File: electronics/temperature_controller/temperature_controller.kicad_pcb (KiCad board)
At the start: 2 copper layers, 139.2 x 91.4 mm, 31 parts, among them J1 Conn_01x03_Male, J2 Conn_01x03_Male, J3 Conn_01x03_Male, J4 Conn_01x03_Male, J5 Conn_01x03_Male, J6 Conn_01x03_Male, K1 RT44xxxx, K2 RT44xxxx, K3 ADW11, K4 ADW11, Q1 2N3904, Q2 2N3904, Q3 2N3904, Q4 2N3904, U1 MC7805CTG, U2 Pico

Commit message: finish board schematics
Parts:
- removed K1, K2: RT44xxxx, Relay_THT:Relay_DPST_Schrack-RT2-FormA_RM5mm
- removed K3, K4: ADW11, Relay_THT:Relay_1P1T_NO_10x24x18.8mm_Panasonic_ADW11xxxxW_THT
- removed RV1, RV2: Varistor, Varistor:RV_Disc_D15.5mm_W4.2mm_P7.5mm
- added D9: 1N5817, Diode_THT:D_DO-41_SOD81_P10.16mm_Horizontal, F.Cu at (160.4, 76.2)
- added H1: MountingHole, MountingHole:MountingHole_3.2mm_M3_Pad_TopBottom, F.Cu at (159.4, 103.3)
- added H2: MountingHole, MountingHole:MountingHole_3.2mm_M3_Pad_TopBottom, F.Cu at (149.9, 111.8)
- added H3: MountingHole, MountingHole:MountingHole_3.2mm_M3_Pad_TopBottom, F.Cu at (172.4, 93.0)
- added H4: MountingHole, MountingHole:MountingHole_3.2mm_M3_Pad_TopBottom, F.Cu at (183.5, 78.1)
- added J10: 1217861-1, ProjectComponents:TE_1217861-1, F.Cu at (77.5, 16.8)
- added J11: 1217861-1, ProjectComponents:TE_1217861-1, F.Cu at (91.9, 16.8)
- added J12: 1217861-1, ProjectComponents:TE_1217861-1, F.Cu at (82.5, 16.8)
- added J13: 1217861-1, ProjectComponents:TE_1217861-1, F.Cu at (86.9, 29.0)
- added J14: 1217861-1, ProjectComponents:TE_1217861-1, F.Cu at (77.2, 29.0)
- added J15: 1217861-1, ProjectComponents:TE_1217861-1, F.Cu at (91.9, 28.7)
- added J16: 1217861-1, ProjectComponents:TE_1217861-1, F.Cu at (81.9, 29.0)
- added J17: Conn_01x03_Male, Connector_PinHeader_2.54mm:PinHeader_1x03_P2.54mm_Vertical, F.Cu at (143.6, 105.7)
- added J18: 1217861-1, ProjectComponents:TE_1217861-1, F.Cu at (134.6, 88.4)
- added J19: 1217861-1, ProjectComponents:TE_1217861-1, F.Cu at (161.6, 97.0)
- added J20: 1217861-1, ProjectComponents:TE_1217861-1, F.Cu at (173.2, 86.7)
- added J21: 1217861-1, ProjectComponents:TE_1217861-1, F.Cu at (174.8, 80.7)
- added J22: Conn_01x15_Male, Connector_PinHeader_2.54mm:PinHeader_1x15_P2.54mm_Vertical, F.Cu at (156.7, 4.32)
- added J23: Conn_01x15_Male, Connector_PinHeader_2.54mm:PinHeader_1x15_P2.54mm_Vertical, F.Cu at (202.2, 4.32)
- added J24: TB006-508-02BE, ProjectComponents:CUI_TB006-508-02BE, F.Cu at (217.7, 33.5)
- added J25: TB006-508-02BE, ProjectComponents:CUI_TB006-508-02BE, F.Cu at (232.6, 15.9)
- added J26: TB006-508-02BE, ProjectComponents:CUI_TB006-508-02BE, F.Cu at (244.3, 15.9)
- added J27: TB006-508-02BE, ProjectComponents:CUI_TB006-508-02BE, F.Cu at (232.6, 26.6)
- added J28: TB006-508-02BE, ProjectComponents:CUI_TB006-508-02BE, F.Cu at (244.3, 26.6)
- added J29: TB006-508-02BE, ProjectComponents:CUI_TB006-508-02BE, F.Cu at (256.0, 15.9)
- added J30: Conn_01x03_Male, Connector_PinHeader_2.54mm:PinHeader_1x03_P2.54mm_Vertical, F.Cu at (230.4, -4.83)
- added J7: 1217861-1, ProjectComponents:TE_1217861-1, F.Cu at (91.7, 40.6)
- added J8: 1217861-1, ProjectComponents:TE_1217861-1, F.Cu at (87.1, 40.6)
- added J9: 1217861-1, ProjectComponents:TE_1217861-1, F.Cu at (87.1, 16.8)
- added Q5: 2N3904, Package_TO_SOT_THT:TO-92_Inline, F.Cu at (155.9, 111.1)
- added Q6: 2N3904, Package_TO_SOT_THT:TO-92_Inline, F.Cu at (165.4, 102.6)
- added R12: 150, Resistor_SMD:R_0805_2012Metric_Pad1.20x1.40mm_HandSolder, F.Cu at (185.3, 93.3)
- added R13: 150, Resistor_SMD:R_0805_2012Metric_Pad1.20x1.40mm_HandSolder, F.Cu at (190.0, 89.1)
- added R14: 10k, Resistor_SMD:R_0805_2012Metric_Pad1.20x1.40mm_HandSolder, F.Cu at (167.6, 114.3)
- added R15: 10k, Resistor_SMD:R_0805_2012Metric_Pad1.20x1.40mm_HandSolder, F.Cu at (178.2, 102.2)
- added R16: 1k, Resistor_SMD:R_0805_2012Metric_Pad1.20x1.40mm_HandSolder, F.Cu at (173.5, 106.9)
- added R17: 1k, Resistor_SMD:R_0805_2012Metric_Pad1.20x1.40mm_HandSolder, F.Cu at (182.9, 99.2)
- added R3: 10k, Resistor_SMD:R_0805_2012Metric_Pad1.20x1.40mm_HandSolder, F.Cu at (178.7, 96.3)
- added R4: 10k, Resistor_SMD:R_0805_2012Metric_Pad1.20x1.40mm_HandSolder, F.Cu at (185.3, 90.3)
- added R5: 1k, Resistor_SMD:R_0805_2012Metric_Pad1.20x1.40mm_HandSolder, F.Cu at (162.8, 114.3)
- added R6: 1k, Resistor_SMD:R_0805_2012Metric_Pad1.20x1.40mm_HandSolder, F.Cu at (172.3, 104.0)
- added R7: 1k, Resistor_SMD:R_0805_2012Metric_Pad1.20x1.40mm_HandSolder, F.Cu at (178.2, 99.2)
- added R8: 1k, Resistor_SMD:R_0805_2012Metric_Pad1.20x1.40mm_HandSolder, F.Cu at (168.7, 106.9)
- added R9: 4k7, Resistor_SMD:R_0805_2012Metric_Pad1.20x1.40mm_HandSolder, F.Cu at (174.8, 75.6)
- added U3: BOB-12009, ProjectComponents:CONV_BOB-12009, F.Cu at (221.8, 18.9)
- C1, C2: footprint Capacitor_THT:C_Rect_L18.0mm_W9.0mm_P15.00mm_FKS3_FKP3 -> Capacitor_THT:C_Disc_D8.0mm_W2.5mm_P5.00mm
- D1, D4: value 1N4148TA -> LED; footprint digikey-footprints:DO-35 -> LED_THT:LED_D3.0mm
- D2, D3: value 1N4148TA -> 1N5817; footprint digikey-footprints:DO-35 -> Diode_THT:D_DO-41_SOD81_P10.16mm_Horizontal
- D7, D8: value LED -> 1N5817; footprint LED_THT:LED_D3.0mm -> Diode_THT:D_DO-41_SOD81_P10.16mm_Horizontal
- J1, J2: value Conn_01x03_Male -> SJ1-3523N; footprint TerminalBlock_Phoenix:TerminalBlock_Phoenix_MKDS-3-3-5.08_1x03_P5.08mm_Horizontal -> ProjectComponents:CUI_SJ1-3523N
- J3: footprint TerminalBlock_Phoenix:TerminalBlock_Phoenix_MKDS-3-3-5.08_1x03_P5.08mm_Horizontal -> Connector_PinHeader_2.54mm:PinHeader_1x03_P2.54mm_Vertical
- J4: value Conn_01x03_Male -> SJ1-3523N; footprint Connector_PinHeader_2.54mm:PinHeader_1x03_P2.54mm_Vertical -> ProjectComponents:CUI_SJ1-3523N
- J5, J6: value Conn_01x03_Male -> 1217861-1; footprint Connector_PinHeader_2.54mm:PinHeader_1x03_P2.54mm_Vertical -> ProjectComponents:TE_1217861-1
- PS1: value IRM-10-12 -> IRM-02-12; footprint Converter_ACDC:Converter_ACDC_MeanWell_IRM-10-xx_THT -> Converter_ACDC:Converter_ACDC_MeanWell_IRM-02-xx_THT
- Q1, Q2: footprint digikey-footprints:TO-92-3 -> Package_TO_SOT_THT:TO-92_Inline
- Q3, Q4: value 2N3904 -> IRF9Z34NPBF; footprint digikey-footprints:TO-92-3 -> Package_TO_SOT_THT:TO-220-3_Vertical
- R1, R2: value R -> 150; footprint Resistor_THT:R_Axial_DIN0516_L15.5mm_D5.0mm_P25.40mm_Horizontal -> Resistor_SMD:R_0805_2012Metric_Pad1.20x1.40mm_HandSolder
- U1: value MC7805CTG -> MC7805CT-BPMS-ND; footprint digikey-footprints:TO-220-3 -> Package_TO_SOT_THT:TO-220-3_Vertical
- U2: value Pico -> NodeMCU1.0(ESP-12E); footprint MCU_RaspberryPi_and_Boards:RPi_Pico_SMD_TH -> ESP8266:NodeMCU1.0(12-E)
- moved J5 173.5 mm to (77.7, 40.7), turned to 90 degrees
- moved R1 170.3 mm to (189.9, 75.6)
- moved R2 151.4 mm to (189.9, 78.5)
- moved J4 147.1 mm to (79.5, 84.3), turned to 0 degrees
- moved C1 123.8 mm to (160.8, 86.4), turned to 0 degrees
- moved PS1 109.6 mm to (106.4, 16.5)
- moved Q2 106.6 mm to (179.9, 86.3), turned to 0 degrees
- moved U2 106.6 mm to (178.8, 22.1), turned to 0 degrees
- moved D5 98.1 mm to (170.7, 85.7), turned to 0 degrees
- moved D1 90.3 mm to (186.1, 84.8), turned to 0 degrees
- moved J2 87.0 mm to (79.5, 99.6), turned to 0 degrees
- moved J6 85.0 mm to (82.4, 40.6), turned to 90 degrees
- moved D2 83.9 mm to (144.8, 90.9), turned to 0 degrees
- moved Q1 82.4 mm to (178.4, 92.3), turned to 0 degrees
- moved J3 82.4 mm to (114.4, 97.6), turned to 0 degrees
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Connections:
- C1 pad 2: Net-(C1-Pad2) -> GND
- C2 pad 1: Net-(C2-Pad1) -> +12V
- C2 pad 2: Net-(C2-Pad2) -> GND
- D5 pad 1: Net-(D2-PadA) -> Net-(D5-Pad1)
- D6 pad 1: Net-(D1-PadA) -> Net-(D6-Pad1)
- D7 pad 1: Net-(D3-PadA) -> +12V
- D7 pad 2: +12V -> Net-(D7-Pad2)
- D8 pad 1: Net-(D8-Pad1) -> +12V
- D8 pad 2: +12V -> Net-(D8-Pad2)
- J1 pad 1: LIVE -> GND
- J1 pad 2: NEUTRAL -> +5V
- J1 pad 3: Earth -> ONEWIRE
- J2 pad 1: Net-(C1-Pad1) -> GND
- J2 pad 2: Net-(J2-Pad2) -> +5V
- J2 pad 3: Earth -> ONEWIRE
- J3 pad 1: Net-(C2-Pad1) -> GND
- J3 pad 2: Net-(J3-Pad2) -> Net-(D2-Pad1)
- J3 pad 3: Earth -> Net-(J3-Pad3)
- J4 pad 2: Net-(J4-Pad2) -> +5V
- J4 pad 3: Net-(J4-Pad3) -> ONEWIRE
- J5 pad 1: GND -> EARTH
- J5 pad 2: Net-(J5-Pad2) -> EARTH
- J6 pad 1: Net-(J6-Pad1) -> EARTH
- J6 pad 2: GND -> EARTH
- Q1 pad 2: Net-(D1-PadA) -> Net-(Q1-Pad2)
- Q1 pad 3: HEAT -> Net-(Q1-Pad3)
- Q2 pad 2: Net-(D2-PadA) -> Net-(Q2-Pad2)
- Q2 pad 3: COOL -> Net-(Q2-Pad3)
- Q3 pad 1: GND -> Net-(Q1-Pad3)
- Q3 pad 2: Net-(D3-PadA) -> Net-(D2-Pad1)
- Q3 pad 3: FAN1 -> +12V
- Q4 pad 1: GND -> Net-(Q2-Pad3)
- Q4 pad 2: Net-(D4-PadA) -> Net-(D3-Pad1)
- Q4 pad 3: FAN2 -> +12V
- R1 pad 1: Net-(C1-Pad2) -> Net-(Q1-Pad2)
- R1 pad 2: Net-(J2-Pad2) -> FAN1
- R2 pad 1: Net-(C2-Pad2) -> Net-(Q2-Pad2)
- R2 pad 2: Net-(J3-Pad2) -> FAN2
- U1 pad 3: +5V -> Net-(C1-Pad1)
- U2 pad 10: Net-(U2-Pad10) -> GND
- U2 pad 12: FAN2 -> Net-(J22-Pad12)
- U2 pad 13: GND -> Net-(J22-Pad13)
- U2 pad 14: Net-(U2-Pad14) -> GND
- U2 pad 15: Net-(U2-Pad15) -> +5V
- U2 pad 17: FAN1 -> GND
- U2 pad 18: GND -> Net-(J23-Pad13)
- U2 pad 20: Net-(U2-Pad20) -> FAN2
- U2 pad 22: Net-(U2-Pad22) -> ONEWIRE
- U2 pad 23: GND -> COOL
- U2 pad 24: COOL -> GND
- U2 pad 26: Net-(U2-Pad26) -> FAN1
- U2 pad 28: GND -> Net-(J23-Pad3)
- U2 pad 29: HEAT -> Net-(J23-Pad2)
- U2 pad 3: GND -> Net-(J22-Pad3)
- U2 pad 30: Net-(U2-Pad30) -> HEAT
- U2 pad 8: GND -> Net-(J22-Pad8)
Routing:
- net LIVE: track 85.6 -> 0.00 mm
- net Net-(J2-Pad2): track 47.3 -> 0.00 mm
- net Net-(C1-Pad1): track 40.5 -> 0.00 mm
- net Net-(J3-Pad2): track 40.3 -> 0.00 mm
- net Net-(C2-Pad1): track 34.9 -> 0.00 mm
- net Net-(C2-Pad2): track 8.23 -> 0.00 mm
- net Net-(C1-Pad2): track 8.23 -> 0.00 mm
- removed copper zone on B.Cu, net Earth
- removed copper zone on B.Cu, net GND
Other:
- board size 139.2 x 91.4 mm -> 1.2 x 12 mm

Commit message: update footprints, schematic and start board layout
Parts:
- removed the J10 at (77.5, 16.8)
- removed the J11 at (91.9, 16.8)
- removed the J12 at (82.5, 16.8)
- removed the J26 at (244.3, 15.9)
- removed J27: TB006-508-02BE, ProjectComponents:CUI_TB006-508-02BE
- removed the J7 at (91.7, 40.6)
- removed the J8 at (87.1, 40.6)
- removed the J9 at (87.1, 16.8)
- added C3: C, Capacitor_THT:C_Disc_D8.0mm_W2.5mm_P5.00mm, F.Cu at (179.8, -11.2)
- added C4: C, Capacitor_THT:C_Disc_D8.0mm_W2.5mm_P5.00mm, F.Cu at (165.9, -0.97)
- added D10: 1N5817, Diode_THT:D_DO-41_SOD81_P10.16mm_Horizontal, F.Cu at (243.1, 84.6)
- added D11: 1N5817, Diode_THT:D_DO-41_SOD81_P10.16mm_Horizontal, F.Cu at (14.0, -15.2)
- added J13: Conn_01x15_Male, Connector_PinHeader_2.54mm:PinHeader_1x15_P2.54mm_Vertical, F.Cu at (57.9, -92.7)
- added J14: SJ1-3523N, ProjectComponents:CUI_SJ1-3523N, F.Cu at (80.3, -4.83)
- added J16: SJ1-3523N, ProjectComponents:CUI_SJ1-3523N, F.Cu at (67.1, -4.83)
- added J17: Conn_01x03_Male, Connector_PinHeader_2.54mm:PinHeader_1x03_P2.54mm_Vertical, F.Cu at (283.8, 89.5)
- added J18: 1217861-1, ProjectComponents:TE_1217861-1, F.Cu at (22.4, -9.40)
- added J21: 1217861-1, ProjectComponents:TE_1217861-1, F.Cu at (30.5, -85.1)
- added J22: 1217861-1, ProjectComponents:TE_1217861-1, F.Cu at (30.7, -90.4)
- added J23: 1217861-1, ProjectComponents:TE_1217861-1, F.Cu at (30.5, -79.0)
- added J30: 1217861-1, ProjectComponents:TE_1217861-1, F.Cu at (19.8, -84.5)
- added J31: 1217861-1, ProjectComponents:TE_1217861-1, F.Cu at (19.8, -96.5)
- added J32: 1217861-1, ProjectComponents:TE_1217861-1, F.Cu at (22.6, -4.06)
- added J33: 1217861-1, ProjectComponents:TE_1217861-1, F.Cu at (4.57, -19.8)
- added J4: 1217861-1, ProjectComponents:TE_1217861-1, F.Cu at (-10.9, 25.7)
- added J40: 1217861-1, ProjectComponents:TE_1217861-1, F.Cu at (6.35, -84.5)
- added J41: 1217861-1, ProjectComponents:TE_1217861-1, F.Cu at (6.35, -78.5)
- added PS1: IRM-10-12, Converter_ACDC:Converter_ACDC_MeanWell_IRM-10-xx_THT, F.Cu at (15.0, -70.0)
- added U4: MC7805CT-BPMS-ND, Package_TO_SOT_THT:TO-220-3_Vertical, F.Cu at (193.8, -19.8)
- D5: renamed from D4; value LED -> 1N5817; footprint LED_THT:LED_D3.0mm -> Diode_THT:D_DO-41_SOD81_P10.16mm_Horizontal
- D7: value 1N5817 -> LED; footprint Diode_THT:D_DO-41_SOD81_P10.16mm_Horizontal -> LED_THT:LED_D3.0mm
- J1: value SJ1-3523N -> Conn_02x03_Odd_Even; footprint ProjectComponents:CUI_SJ1-3523N -> Connector_PinHeader_2.54mm:PinHeader_2x03_P2.54mm_Vertical
- J15: value 1217861-1 -> SJ1-3523N; footprint ProjectComponents:TE_1217861-1 -> ProjectComponents:CUI_SJ1-3523N
- J19: renamed from J22; value Conn_01x15_Male -> 1217861-1; footprint Connector_PinHeader_2.54mm:PinHeader_1x15_P2.54mm_Vertical -> ProjectComponents:TE_1217861-1
- J2: value SJ1-3523N -> Conn_01x03_Male; footprint ProjectComponents:CUI_SJ1-3523N -> Connector_PinHeader_2.54mm:PinHeader_1x03_P2.54mm_Vertical
- J24, J25, J28, J29: value TB006-508-02BE -> 1217861-1; footprint ProjectComponents:CUI_TB006-508-02BE -> ProjectComponents:TE_1217861-1
- J26: renamed from J23; value Conn_01x15_Male -> 1217861-1; footprint Connector_PinHeader_2.54mm:PinHeader_1x15_P2.54mm_Vertical -> ProjectComponents:TE_1217861-1
- J3: renamed from J4; value SJ1-3523N -> Conn_02x08_Odd_Even; footprint ProjectComponents:CUI_SJ1-3523N -> Connector_PinHeader_2.54mm:PinHeader_2x08_P2.54mm_Vertical
- J39: renamed from J30; value Conn_01x03_Male -> 1217861-1; footprint Connector_PinHeader_2.54mm:PinHeader_1x03_P2.54mm_Vertical -> ProjectComponents:TE_1217861-1
- J6: value 1217861-1 -> Conn_01x03_Male; footprint ProjectComponents:TE_1217861-1 -> Connector_PinHeader_2.54mm:PinHeader_1x03_P2.54mm_Vertical
- J8: renamed from J17; value Conn_01x03_Male -> Conn_01x15_Male; footprint Connector_PinHeader_2.54mm:PinHeader_1x03_P2.54mm_Vertical -> Connector_PinHeader_2.54mm:PinHeader_1x15_P2.54mm_Vertical
- R11: renamed from R13; value 150 -> 10k
- R13: renamed from R15; value 10k -> 1k
- R15: renamed from R17; value 1k -> 4k7
- R7: value 1k -> 1k (DNP)
- R9: value 4k7 -> 150
- U1: renamed from U2; value NodeMCU1.0(ESP-12E) -> LD1117S33TR_SOT223; footprint ESP8266:NodeMCU1.0(12-E) -> Package_TO_SOT_SMD:SOT-223-3_TabPin2
- U2: renamed from U1; value MC7805CT-BPMS-ND -> NodeMCU1.0(ESP-12E); footprint Package_TO_SOT_THT:TO-220-3_Vertical -> ESP8266:NodeMCU1.0(12-E)
- moved J29 259.0 mm to (19.8, -90.5), turned to 180 degrees
- moved J28 247.8 mm to (19.8, -78.5), turned to 180 degrees
- moved J39 243.1 mm to (5.33, -96.8), turned to 180 degrees
- moved J24 227.7 mm to (30.7, -96.5), turned to 180 degrees
- moved J25 226.3 mm to (7.11, -3.81)
- moved J5 219.5 mm to (293.4, 81.6), turned to 0 degrees
- moved J6 214.0 mm to (293.4, 76.9), turned to 0 degrees
- moved U3 207.8 mm to (46.2, -92.2), turned to 90 degrees
- moved J11 199.3 mm to (-11.2, 10.9), turned to 180 degrees
- moved J10 198.1 mm to (-10.9, -0.25)
- moved J26 195.3 mm to (7.37, -9.40), turned to 180 degrees
- moved J8 174.6 mm to (57.9, -46.5), turned to 90 degrees
- moved U2 173.5 mm to (75.7, -68.3), turned to 90 degrees
- moved J9 167.9 mm to (-11.2, 5.08), turned to 180 degrees
- moved D3 155.9 mm to (54.4, -36.1), turned to 180 degrees
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- renumbered D5 to D1, D1 to D2, D2 to D3, D3 to D4, J19 to J10, J20 to J11, J21 to J12, J13 to J35, J14 to J36, J16 to J38, J3 to J7, J18 to J9, PS1 to PS2, R12 to R10, R14 to R12, R16 to R14
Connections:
- C1 pad 1: Net-(C1-Pad1) -> +12V
- C2 pad 1: +12V -> Net-(C2-Pad1)
- D1 pad 2: +12V -> Net-(D1-Pad2)
- D3 pad 1: Net-(D2-Pad1) (its old number) -> +3V3
- D3 pad 2: GND -> Net-(C2-Pad1)
- D4 pad 1: Net-(D3-Pad1) -> Net-(D4-Pad1)
- D5 pad 1: Net-(D4-Pad1) -> Net-(D5-Pad1)
- D5 pad 2: +12V -> GND
- D7 pad 1: +12V -> Net-(D7-Pad1)
- D7 pad 2: Net-(D7-Pad2) -> +12V
- D9 pad 1: +5V -> +12V
- D9 pad 2: Net-(C1-Pad1) -> Net-(D9-Pad2)
- J1 pad 1: GND -> AUXO
- J1 pad 2: +5V -> AUXO
- J1 pad 3: ONEWIRE -> Net-(J1-Pad3)
- J10 pad 1: Net-(D7-Pad2) -> Net-(D8-Pad2)
- J10 pad 2: Net-(D7-Pad2) -> Net-(D8-Pad2)
- J12 pad 1: Net-(D8-Pad2) -> Net-(D9-Pad2)
- J12 pad 2: Net-(D8-Pad2) -> Net-(D9-Pad2)
- J15 pad 1: LIVE -> GND
- J15 pad 2: LIVE -> +5V
- J19 pad 1: Net-(J22-Pad1) -> GND
- J19 pad 2: Net-(J22-Pad2) -> GND
- J2 pad 1: GND -> +5V
- J2 pad 2: +5V -> Net-(D1-Pad2)
- J2 pad 3: ONEWIRE -> +12V
- J24 pad 1: +5V -> EARTH
- J24 pad 2: GND -> EARTH
- J25 pad 2: GND -> +5V
- J26 pad 1: HEAT -> +5V
- J26 pad 2: Net-(J23-Pad2) -> +5V
- J28 pad 1: +12V -> NEUTRAL
- J28 pad 2: GND -> NEUTRAL
- J29 pad 1: +12V -> NEUTRAL
- J29 pad 2: GND -> NEUTRAL
- J3 pad 2: +5V -> +3V3
- J3 pad 3: ONEWIRE -> Net-(J1-Pad3)
- J35 pad 1: LIVE -> +12V
- J35 pad 2: LIVE -> +12V
- J36 pad 1: LIVE -> +12V
- J36 pad 2: LIVE -> +12V
- J39 pad 1: +5V -> LIVE
- J39 pad 2: Net-(J30-Pad2) -> LIVE
- J5 pad 1: EARTH -> GND
- J5 pad 2: EARTH -> GND
- J6 pad 1: EARTH -> GND
- J6 pad 2: EARTH -> Net-(D4-Pad1)
- J7 pad 2: Net-(D2-Pad1) (its old number) -> Net-(D5-Pad1)
- J8 pad 1: GND -> Net-(J8-Pad1)
- J8 pad 2: Net-(D3-Pad1) -> Net-(J8-Pad2)
- J8 pad 3: Net-(J17-Pad3) -> Net-(J8-Pad3)
- PS2 pad 4: +12V -> Net-(D11-Pad2)
- Q3 pad 2: Net-(D2-Pad1) (its old number) -> Net-(D4-Pad1)
- Q3 pad 3: +12V -> Net-(D1-Pad2)
- Q4 pad 2: Net-(D3-Pad1) -> Net-(D5-Pad1)
- Q5 pad 3: Net-(D7-Pad2) -> Net-(D8-Pad2)
- Q6 pad 3: Net-(D8-Pad2) -> Net-(D9-Pad2)
- R1 pad 2: FAN1 -> AUX0
- R10 pad 1: Net-(Q5-Pad2) -> Net-(Q6-Pad2)
- R10 pad 2: HEAT -> COOL
- R11 pad 1: Net-(Q6-Pad2) -> GND
- R11 pad 2: COOL -> Net-(Q5-Pad2)
- R12 pad 2: Net-(Q5-Pad2) -> Net-(Q6-Pad2)
- R13 pad 1: GND -> Net-(D6-Pad1)
- R13 pad 2: Net-(Q6-Pad2) -> Net-(D8-Pad2)
- R14 pad 1: Net-(D4-Pad1) -> Net-(D7-Pad1)
- R14 pad 2: Net-(D7-Pad2) -> Net-(D9-Pad2)
- R15 pad 1: Net-(D6-Pad1) -> +5V
- R15 pad 2: Net-(D8-Pad2) -> ONEWIRE
- R2 pad 2: FAN2 -> FAN
- R7 pad 2: +12V -> Net-(D1-Pad2)
- R9 pad 1: +5V -> Net-(Q5-Pad2)
- R9 pad 2: ONEWIRE -> HEAT
- U1 pad 1: Net-(J22-Pad1) -> GND
- U1 pad 2: Net-(J22-Pad2) -> Net-(C2-Pad1)
- U1 pad 3: Net-(J22-Pad3) -> +12V
- U2 pad 1: +12V -> Net-(J8-Pad1)
- U2 pad 2: GND -> Net-(J8-Pad2)
- U2 pad 3: Net-(C1-Pad1) -> Net-(J8-Pad3)
- U3 pad HV: Net-(J30-Pad2) -> Net-(J17-Pad2)
- U3 pad LV: Net-(J23-Pad6) -> Net-(J13-Pad6)
- U3 pad LV1: Net-(J23-Pad2) -> SCL
- U3 pad LV2: Net-(J23-Pad3) -> SDA
- U3 pad LV3: Net-(J23-Pad4) -> Net-(J13-Pad4)
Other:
- board size 1.2 x 12 mm -> 100 x 100 mm

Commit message: finished layout move to bluetooth shield
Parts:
- removed C1, C2: C, Capacitor_THT:C_Disc_D8.0mm_W2.5mm_P5.00mm
- removed D11: 1N5817, Diode_THT:D_DO-41_SOD81_P10.16mm_Horizontal
- removed J13, J8: Conn_01x15_Male, Connector_PinHeader_2.54mm:PinHeader_1x15_P2.54mm_Vertical
- removed J18, J19: 1217861-1, ProjectComponents:TE_1217861-1
- removed U1: LD1117S33TR_SOT223, Package_TO_SOT_SMD:SOT-223-3_TabPin2
- D10, D3, D4, D5, D8, D9: value 1N5817 -> ‎DSS13UTR‎; footprint Diode_THT:D_DO-41_SOD81_P10.16mm_Horizontal -> ProjectComponents:D_SOD-123F
- moved J6 271.3 mm to (85.0, -96.9), turned to 270 degrees
- moved J17 257.5 mm to (81.3, -69.6), turned to 270 degrees
- moved J5 257.5 mm to (97.0, -85.0), turned to 90 degrees
- moved D5 253.6 mm to (44.9, -95.0), turned to 270 degrees
- moved H2 252.6 mm to (5.00, -95.0)
- moved R14 241.6 mm to (51.6, -81.0)
- moved R12 241.2 mm to (51.6, -77.0)
- moved Q5 240.1 mm to (43.9, -85.0), turned to 90 degrees
- moved Q3 238.4 mm to (85.0, -92.1), turned to 180 degrees
- moved D10 237.1 mm to (28.8, -17.0), turned to 90 degrees
- moved R8 233.4 mm to (69.5, -85.2), turned to 180 degrees
- moved R13 230.7 mm to (37.9, -81.0)
- moved R5 229.5 mm to (88.0, -85.3)
- moved D6 229.1 mm to (38.9, -87.0), turned to 180 degrees
- moved R11 225.2 mm to (37.9, -77.0)
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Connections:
- net Net-(J3-Pad10) renamed MISO
- net Net-(J3-Pad12) renamed SCLK
- net Net-(J3-Pad6) renamed MOSI
- net Net-(J3-Pad8) renamed CS
- D10 pad 1: +5V -> +12V
- D10 pad 2: Net-(C3-Pad1) -> Net-(D10-Pad2)
- D3 pad 1: +3V3 -> Net-(D3-Pad1)
- D3 pad 2: Net-(C2-Pad1) -> GND
- D5 pad 1: Net-(D5-Pad1) -> +12V
- D5 pad 2: GND -> Net-(D5-Pad2)
- D9 pad 1: +12V -> +5V
- D9 pad 2: Net-(D9-Pad2) -> Net-(C3-Pad1)
- J10 pad 1: Net-(D8-Pad2) -> Net-(D5-Pad2)
- J10 pad 2: Net-(D8-Pad2) -> Net-(D5-Pad2)
- J12 pad 1: Net-(D9-Pad2) -> Net-(D8-Pad2)
- J12 pad 2: Net-(D9-Pad2) -> Net-(D8-Pad2)
- J3 pad 14: GND -> +12V
- J3 pad 15: +3V3 -> +5V
- J3 pad 2: +3V3 -> +12V
- J3 pad 9: +3V3 -> +5V
- J4 pad 1: Net-(D4-Pad1) -> Net-(D3-Pad1)
- J4 pad 2: Net-(D4-Pad1) -> Net-(D3-Pad1)
- J6 pad 2: Net-(D4-Pad1) -> Net-(D3-Pad1)
- J7 pad 2: Net-(D5-Pad1) -> Net-(D4-Pad1)
- PS1 pad 4: Net-(D11-Pad2) -> Net-(D10-Pad2)
- PS2 pad 4: Net-(D11-Pad2) -> Net-(D10-Pad2)
- Q3 pad 2: Net-(D4-Pad1) -> Net-(D3-Pad1)
- Q4 pad 2: Net-(D5-Pad1) -> Net-(D4-Pad1)
- Q5 pad 3: Net-(D8-Pad2) -> Net-(D5-Pad2)
- Q6 pad 3: Net-(D9-Pad2) -> Net-(D8-Pad2)
- R1 pad 2: AUX0 -> AUXO
- R13 pad 2: Net-(D8-Pad2) -> Net-(D5-Pad2)
- R14 pad 2: Net-(D9-Pad2) -> Net-(D8-Pad2)
- U2 pad 26: FAN1 -> FAN
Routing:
- net +12V: track 0.00 -> 305.8 mm
- net +5V: track 0.00 -> 255.5 mm
- net LIVE: track 0.00 -> 236.0 mm
- net NEUTRAL: track 0.00 -> 231.0 mm
- net EARTH: track 0.00 -> 145.8 mm
- net ONEWIRE: track 0.00 -> 101.1 mm
- net AUXO: track 0.00 -> 83.7 mm
- net SCL: track 0.00 -> 70.3 mm, vias 0 -> 1
- net SDA: track 0.00 -> 62.5 mm, vias 0 -> 1
- net FAN: track 0.00 -> 51.2 mm
- net AUXIO: track 0.00 -> 41.3 mm
- net COOL: track 0.00 -> 40.9 mm
- net HEAT: track 0.00 -> 35.4 mm
- net Net-(Q2-Pad3): track 0.00 -> 33.8 mm
- net Net-(D3-Pad1): track 0.00 -> 27.6 mm
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- added copper zone on B.Cu, net GND
- added copper zone on F.Cu, net GND

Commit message: Updating layouts and schematics and reading for export
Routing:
- net GND: vias 43 -> 40
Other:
- board size 100 x 100 mm -> 99.8 x 99.8 mm
- board text added: "COOL"
- board text added: "HEAT"

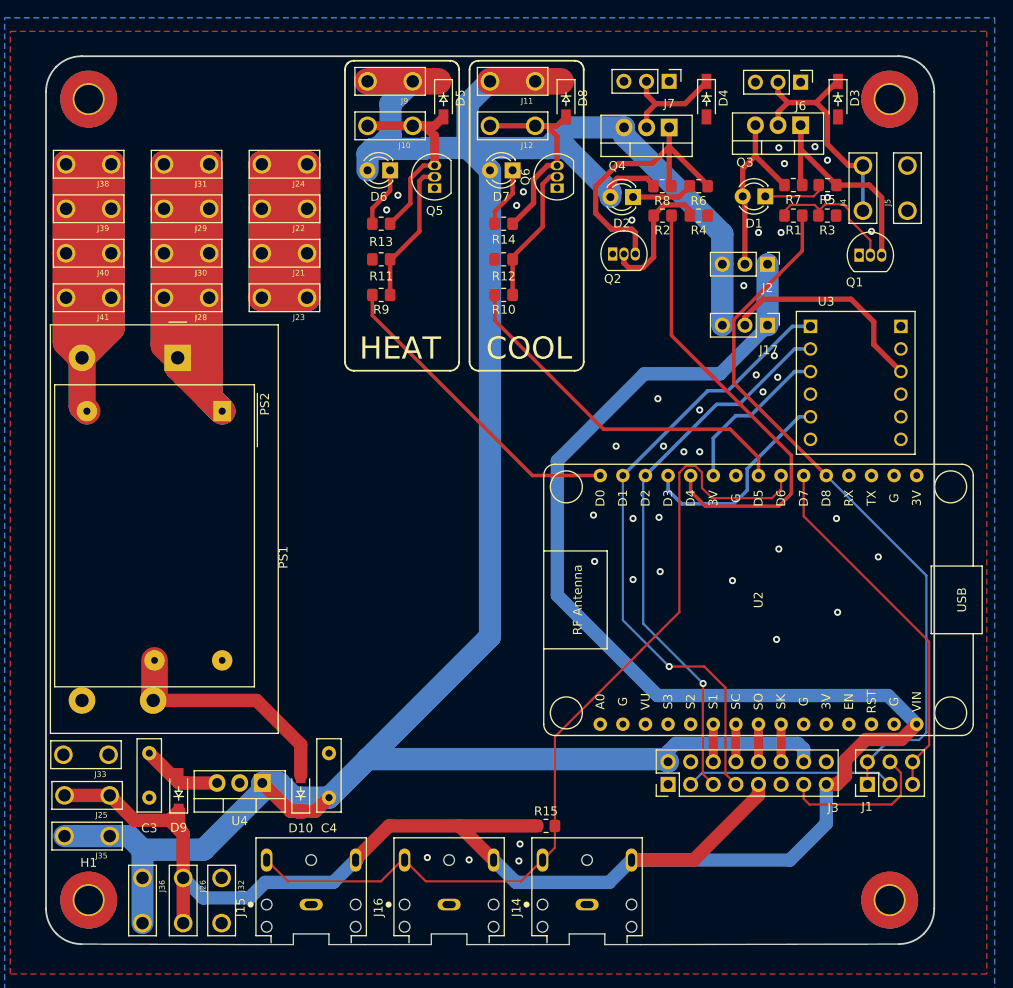
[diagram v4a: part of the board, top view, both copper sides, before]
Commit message: Updating layouts for better shield addition
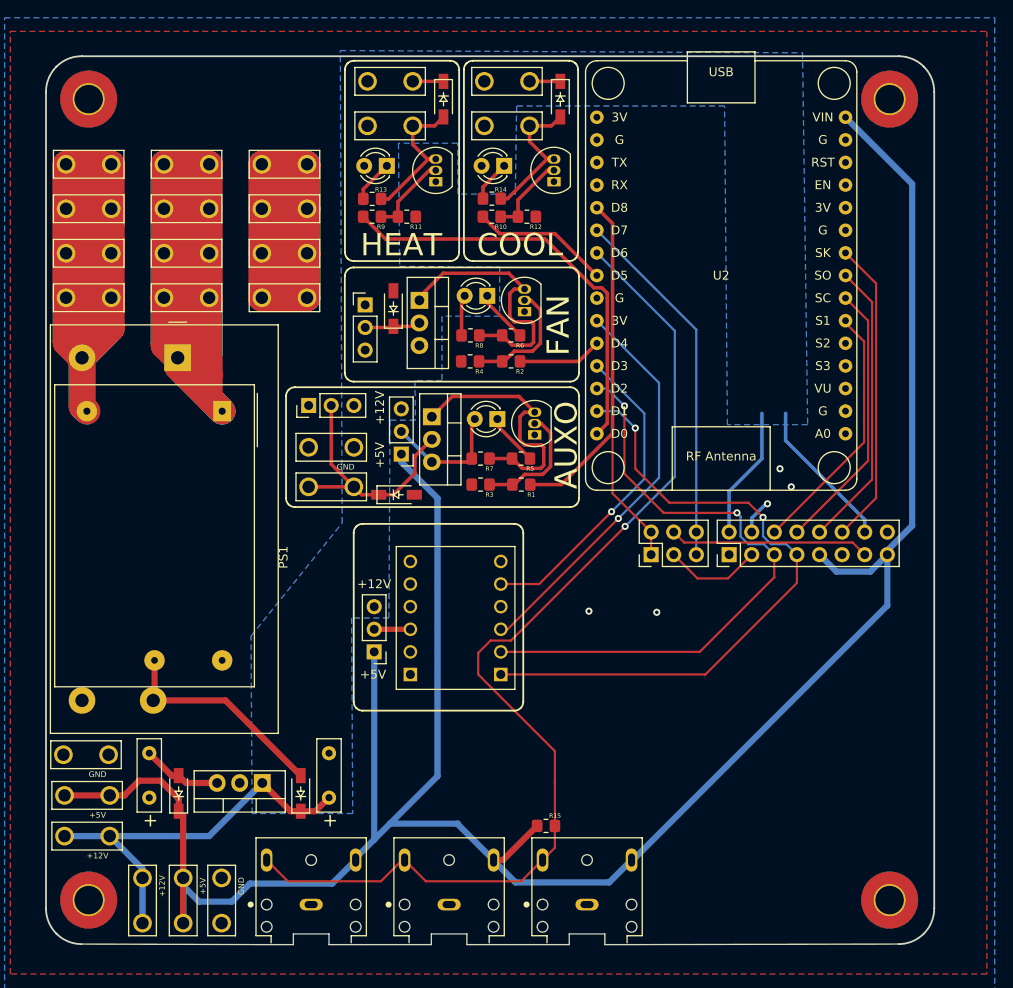
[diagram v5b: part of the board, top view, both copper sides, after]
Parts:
- removed J5: 1217861-1, ProjectComponents:TE_1217861-1
- added ?: , , F.Cu at (128.9, -26.3)
- added ?: , , F.Cu at (130.7, -25.5)
- added GND: 1217861-1, ProjectComponents:TE_1217861-1, F.Cu at (32.3, -55.9)
- R8: value 1k -> DNP
- moved J4 68.5 mm to (32.3, -51.4), turned to 180 degrees
- moved D3 66.6 mm to (39.6, -50.5), turned to 0 degrees
- moved J6 66.1 mm to (29.7, -60.6), turned to 90 degrees
- moved J17 57.4 mm to (37.1, -32.9), turned to 180 degrees
- moved Q3 52.8 mm to (43.6, -59.3), turned to 270 degrees
- moved U3 52.1 mm to (46.2, -36.7), turned to 180 degrees
- moved R3 49.3 mm to (49.0, -51.7), turned to 0 degrees
- moved R7 46.7 mm to (49.0, -54.6)
- moved J2 46.4 mm to (40.1, -55.1), turned to 180 degrees
- moved R5 46.2 mm to (53.6, -54.6), turned to 180 degrees
- moved R1 43.0 mm to (53.6, -51.7)
- moved J7 42.4 mm to (36.1, -71.9), turned to 0 degrees
- moved D4 42.3 mm to (39.2, -71.5), turned to 90 degrees
- moved Q1 41.7 mm to (55.1, -57.3), turned to 90 degrees
- moved D1 39.1 mm to (50.9, -59.1)
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- renumbered J36 to +12V, J35 to +12V, J26 to +5V, J25 to +5V, J33 to GND, J32 to GND
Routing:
- net +12V: track 305.8 -> 88.8 mm
- net FAN: track 51.2 -> 9.48 mm
- net AUXO: track 83.7 -> 53.2 mm
- net SCLK: track 4.23 -> 34.4 mm
- net MISO: track 4.23 -> 32.5 mm
- net Net-(U2-Pad25): track 18.2 -> 45.4 mm, vias 0 -> 1
- net CS: track 4.23 -> 30.7 mm
- net COOL: track 40.9 -> 15.5 mm
- net MOSI: track 4.23 -> 28.8 mm
- net ONEWIRE: track 101.1 -> 121.9 mm, vias 0 -> 1
- net Net-(J17-Pad2): track 24.1 -> 4.06 mm
- net +5V: track 255.5 -> 273.4 mm
- net Net-(J1-Pad3): track 23.5 -> 11.0 mm
- net Net-(U2-Pad27): track 23.7 -> 35.9 mm, vias 0 -> 1
- net HEAT: track 35.4 -> 47.3 mm
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- added copper zone on B.Cu, net +12V
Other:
- board text added: "+"
- board text added: "+12V"
- board text added: "+5V"
- board text added: "AUXO"
- board text added: "FAN"
